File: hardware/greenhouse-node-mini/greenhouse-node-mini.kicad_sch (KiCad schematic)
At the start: 40 parts, among them J1 Molex_KK_396_1x2, J2 JST_XH_2.54mm_1x2, J4 Molex_KK_396_1x2, J5 JST_XH_2.54mm_1x4, J6 PinHeader_1x04_P2.54mm, J7 PinHeader_1x04_P2.54mm, Q1 A42, U1 ATtiny84A-P, U2 L7805, U3 PCF8574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

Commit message: Swapped GND/PWR for IC programming connector
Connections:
- net +5V: now also J2.2 (Pin_2); no longer J2.1 (Pin_1)
- net GND: now also J2.1 (Pin_1); no longer J2.2 (Pin_2)
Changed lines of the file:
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@@
     (pin "1")
+  )
+  (symbol (lib_id "Connector:Conn_01x02_Male") (at 45.72 62.23 0) (mirror x) (unit 1)
+    (in_bom yes) (on_board yes) (fields_autoplaced)
+    (property "Reference" "J2" (id 0) (at 44.45 59.6899 0)
+      (effects (font (size 1.27 1.27)) (justify right))
+    )
+    (property "Value" "JST_XH_2.54mm_1x2" (id 1) (at 44.45 62.2299 0)
+      (effects (font (size 1.27 1.27)) (justify right))
+    )
+    (property "Footprint" "Connector_JST:JST_XH_B2B-XH-A_1x02_P2.50mm_Vertical" (id 2) (at 45.72 62.23 0)
+      (effects (font (size 1.27 1.27)) hide)
+    )
+    (property "Datasheet" "~" (id 3) (at 45.72 62.23 0)
+      (effects (font (size 1.27 1.27)) hide)
+    )
+    (pin "1")
+    (pin "2")
   )
   (symbol (lib_id "power:GND") (at 227.33 133.35 0) (unit 1)
@@
     (pin "2")
   )
-  (symbol (lib_id "Connector:Conn_01x02_Male") (at 45.72 59.69 0) (unit 1)
-    (in_bom yes) (on_board yes) (fields_autoplaced)
-    (property "Reference" "J2" (id 0) (at 46.355 54.61 0))
-    (property "Value" "JST_XH_2.54mm_1x2" (id 1) (at 46.355 57.15 0))
-    (property "Footprint" "Connector_JST:JST_XH_B2B-XH-A_1x02_P2.50mm_Vertical" (id 2) (at 45.72 59.69 0)
-      (effects (font (size 1.27 1.27)) hide)
-    )
-    (property "Datasheet" "~" (id 3) (at 45.72 59.69 0)
-      (effects (font (size 1.27 1.27)) hide)
-    )
-    (pin "1")
-    (pin "2")
-  )
   (symbol (lib_id "Device:R_Small_US") (at 259.08 148.59 270) (mirror x) (unit 1)
     (in_bom yes) (on_board yes) (fields_autoplaced)
@@
       (reference "J1") (unit 1) (value "Molex_KK_396_1x2") (footprint "Connector_Molex:Molex_KK-396_A-41791-0002_1x02_P3.96mm_Vertical")
     )
-    (path "/ea9fe40b-c59e-4c0b-9cb7-bdacd16d2c47"
+    (path "/d9d1085b-9b15-4340-9b95-610882d9fee3"
       (reference "J2") (unit 1) (value "JST_XH_2.54mm_1x2") (footprint "Connector_JST:JST_XH_B2B-XH-A_1x02_P2.50mm_Vertical")
     )

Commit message: Set IO address to 0x20/0x65/0x64
According to internet, 0x20
According to datasheet, 0x65/0x64
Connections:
- net GND: now also U3.1 (A0), U3.2 (A1), U3.3 (A2)
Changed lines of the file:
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@@
   (junction (at 101.6 78.74) (diameter 0) (color 0 0 0 0)
   )
+  (junction (at 147.32 100.33) (diameter 0) (color 0 0 0 0)
+  )
   (junction (at 168.91 30.48) (diameter 0) (color 0 0 0 0)
   )
@@
   (junction (at 57.15 161.29) (diameter 0) (color 0 0 0 0)
   )
+  (junction (at 147.32 102.87) (diameter 0) (color 0 0 0 0)
+  )
   (junction (at 57.15 151.13) (diameter 0) (color 0 0 0 0)
   )
@@
     (stroke (width 0) (type default) (color 0 0 0 0))
   )
+  (wire (pts (xy 147.32 102.87) (xy 153.67 102.87))
+    (stroke (width 0) (type default) (color 0 0 0 0))
+  )
   (wire (pts (xy 255.27 55.88) (xy 266.7 55.88))
     (stroke (width 0) (type default) (color 0 0 0 0))
@@
     (stroke (width 0) (type default) (color 0 0 0 0))
   )
+  (wire (pts (xy 153.67 100.33) (xy 147.32 100.33))
+    (stroke (width 0) (type default) (color 0 0 0 0))
+  )
   (wire (pts (xy 113.03 38.1) (xy 113.03 46.99))
     (stroke (width 0) (type default) (color 0 0 0 0))
@@
     (stroke (width 0) (type default) (color 0 0 0 0))
   )
+  (wire (pts (xy 147.32 97.79) (xy 147.32 100.33))
+    (stroke (width 0) (type default) (color 0 0 0 0))
+  )
   (wire (pts (xy 57.15 151.13) (xy 57.15 140.97))
     (stroke (width 0) (type default) (color 0 0 0 0))
@@
     (stroke (width 0) (type default) (color 0 0 0 0))
   )
+  (wire (pts (xy 147.32 100.33) (xy 147.32 102.87))
+    (stroke (width 0) (type default) (color 0 0 0 0))
+  )
   (wire (pts (xy 175.26 22.86) (xy 175.26 24.13))
     (stroke (width 0) (type default) (color 0 0 0 0))
@@
     (stroke (width 0) (type default) (color 0 0 0 0))
   )
+  (wire (pts (xy 147.32 104.14) (xy 147.32 102.87))
+    (stroke (width 0) (type default) (color 0 0 0 0))
+  )
   (wire (pts (xy 200.66 100.33) (xy 200.66 97.79))
     (stroke (width 0) (type default) (color 0 0 0 0))
@@
   )
   (wire (pts (xy 110.49 46.99) (xy 113.03 46.99))
+    (stroke (width 0) (type default) (color 0 0 0 0))
+  )
+  (wire (pts (xy 153.67 97.79) (xy 147.32 97.79))
     (stroke (width 0) (type default) (color 0 0 0 0))
   )
@@
     (pin "2")
   )
+  (symbol (lib_id "power:GND") (at 147.32 104.14 0) (unit 1)
+    (in_bom yes) (on_board yes) (fields_autoplaced)
+    (property "Reference" "#PWR?" (id 0) (at 147.32 110.49 0)
+      (effects (font (size 1.27 1.27)) hide)
+    )
+    (property "Value" "GND" (id 1) (at 147.32 109.22 0))
+    (property "Footprint" "" (id 2) (at 147.32 104.14 0)
+      (effects (font (size 1.27 1.27)) hide)
+    )
+    (property "Datasheet" "" (id 3) (at 147.32 104.14 0)
+      (effects (font (size 1.27 1.27)) hide)
+    )
+    (pin "1")
+  )
   (symbol (lib_id "power:GND") (at 252.73 130.81 0) (unit 1)
     (in_bom yes) (on_board yes) (fields_autoplaced)
@@
       (reference "#PWR0112") (unit 1) (value "GND") (footprint "")
     )
+    (path "/50bae16a-a78d-43ed-9cff-a3bd02aff6fa"
+      (reference "#PWR?") (unit 1) (value "GND") (footprint "")
+    )
     (path "/695ccbcc-4a44-4a1f-b5e4-e7c0459755d8"

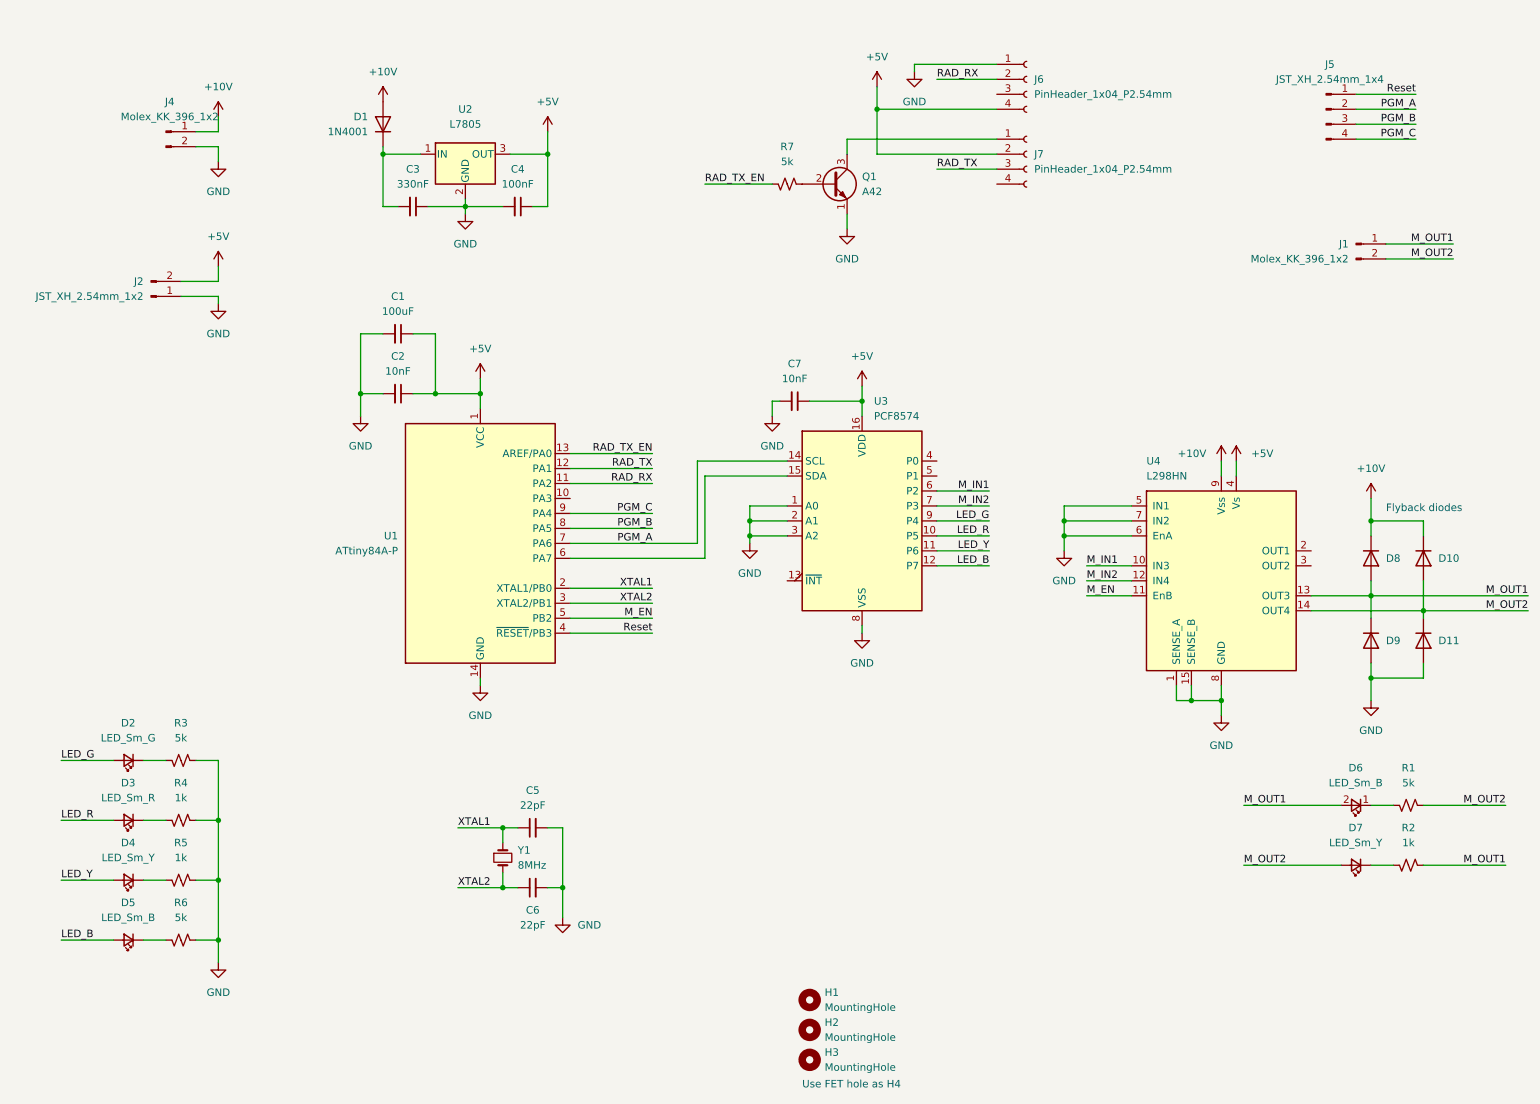
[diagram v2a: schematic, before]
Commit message: Add I2C pull-ups
Also reorganised schematic
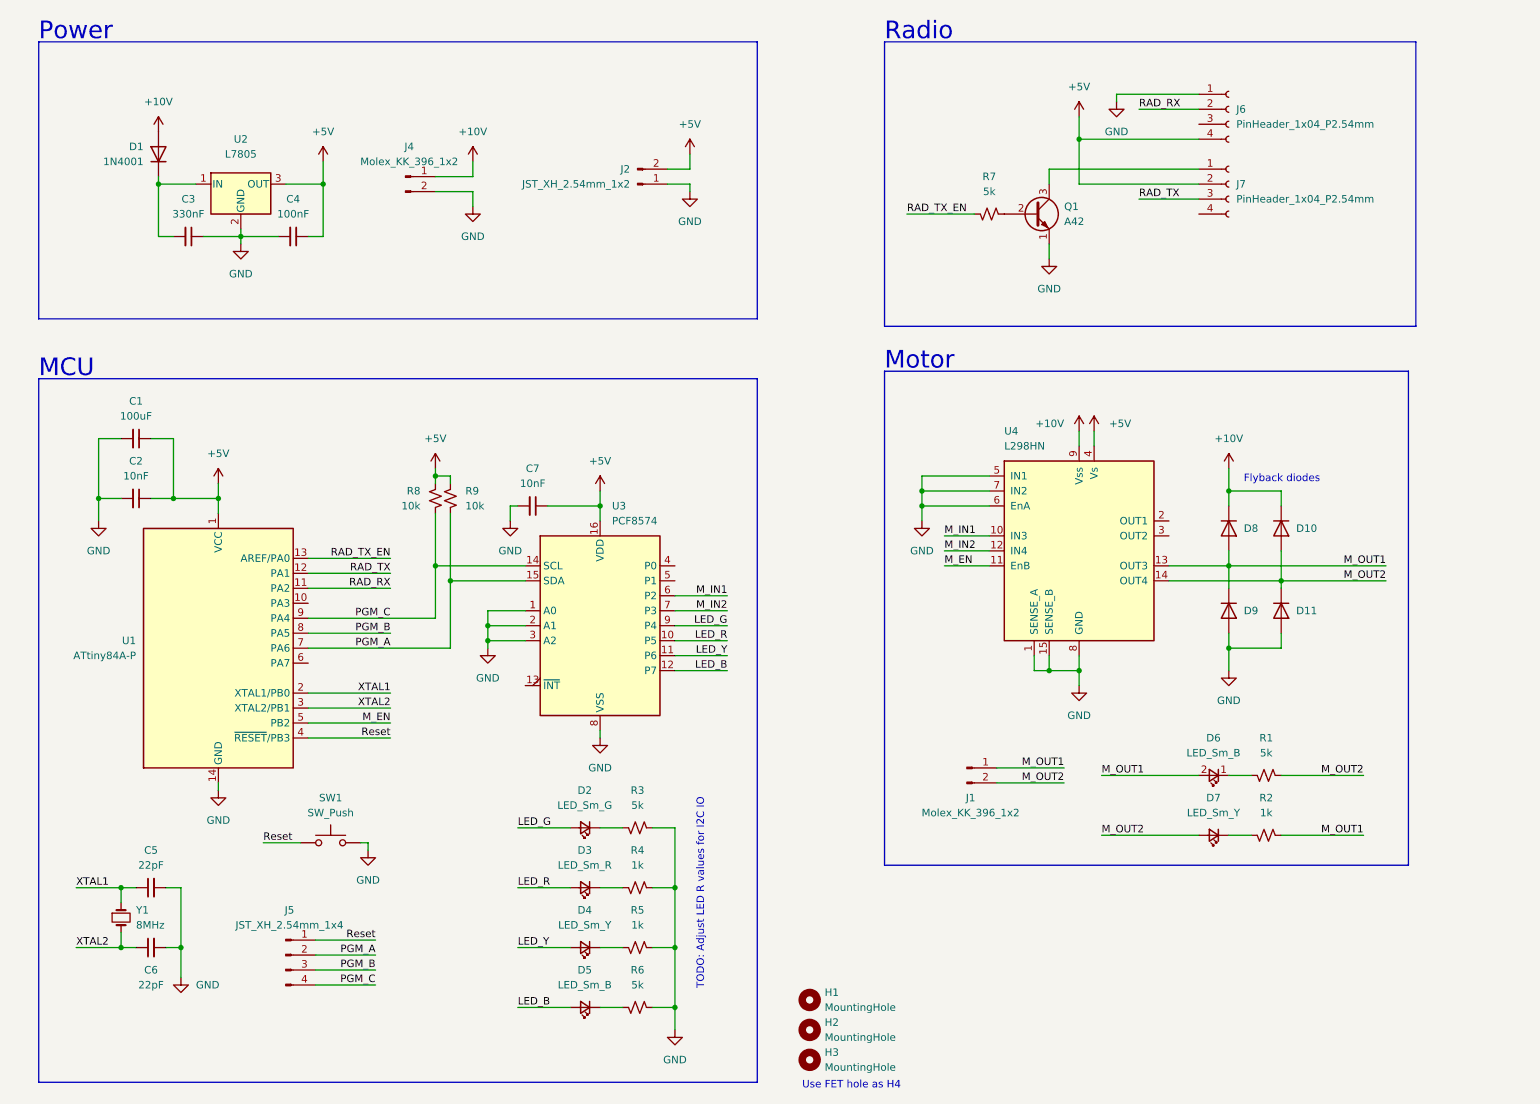
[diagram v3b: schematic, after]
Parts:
- added R8, R9: 10k, Resistor_THT:R_Axial_DIN0204_L3.6mm_D1.6mm_P7.62mm_Horizontal, symbol Device:R_Small_US
- added SW1: SW_Push, Button_Switch_THT:SW_PUSH_6mm, symbol Switch:SW_Push
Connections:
- net +5V: now also R8.1, R9.1
- net GND: now also SW1.2
- net PGM_A: now also U3.15 (SDA), R9.2; no longer U3.14 (SCL)
- net PGM_C: now also U3.14 (SCL), R8.2
- net Reset: now also SW1.1
- net at U1.6 (PA7): no longer U3.15 (SDA)
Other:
- note added: "MCU"
- note added: "Motor"
- note added: "Power"
- note added: "Radio"
- note added: "TODO: Adjust LED R values for I2C IO"
- company: (none) -> Nick Bolton
- title: (none) -> Greenhouse Node Mini
- moved on the sheet: C1, C2, C3, C4, C5, C6, C7, D1, D10, D11, D2, D3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

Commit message: Change LEDs to current sink (PCB WIP)
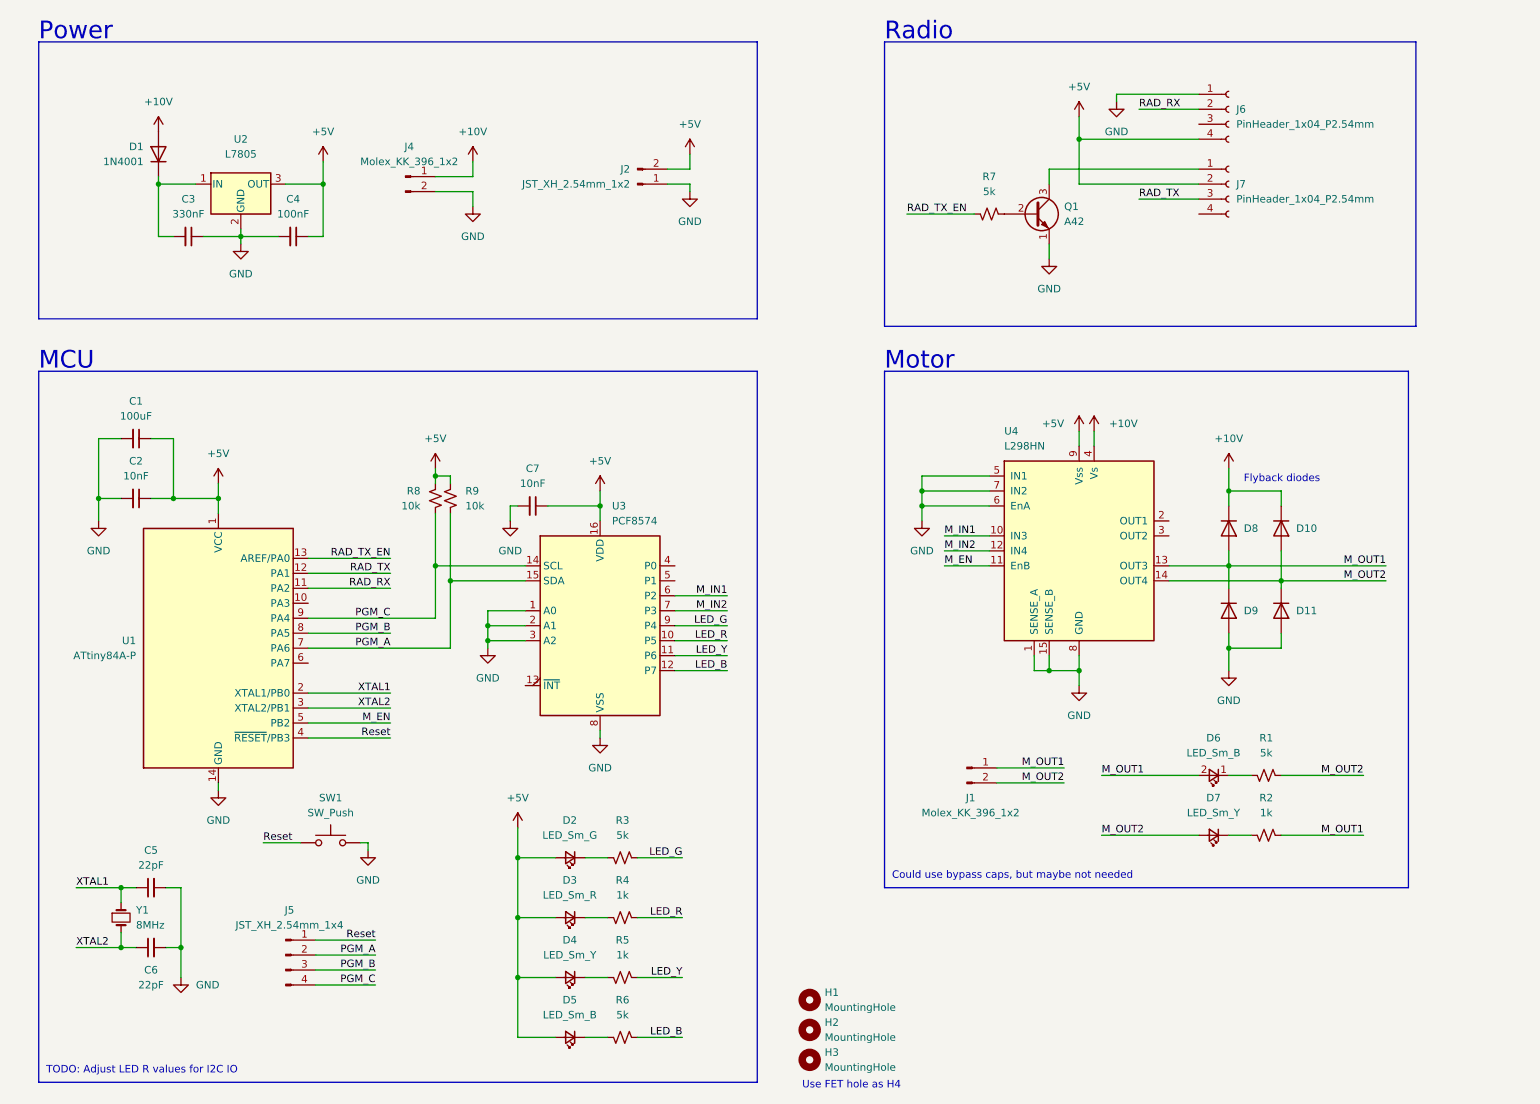
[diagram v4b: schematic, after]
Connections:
- net +10V: now also U4.4 (Vs); no longer U4.9 (Vss)
- net +5V: now also D2.2 (A), D3.2 (A), D4.2 (A), D5.2 (A), U4.9 (Vss); no longer U4.4 (Vs)
- net GND: no longer R3.1, R4.1, R5.1, R6.1
- net LED_B: now also R6.1; no longer D5.2 (A)
- net LED_G: now also R3.1; no longer D2.2 (A)
- net LED_R: now also R4.1; no longer D3.2 (A)
- net LED_Y: now also R5.1; no longer D4.2 (A)
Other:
- note added: "Could use bypass caps, but maybe not needed"
- moved on the sheet: D2, D3, D4, D5

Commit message: Change diodes to fast recovery
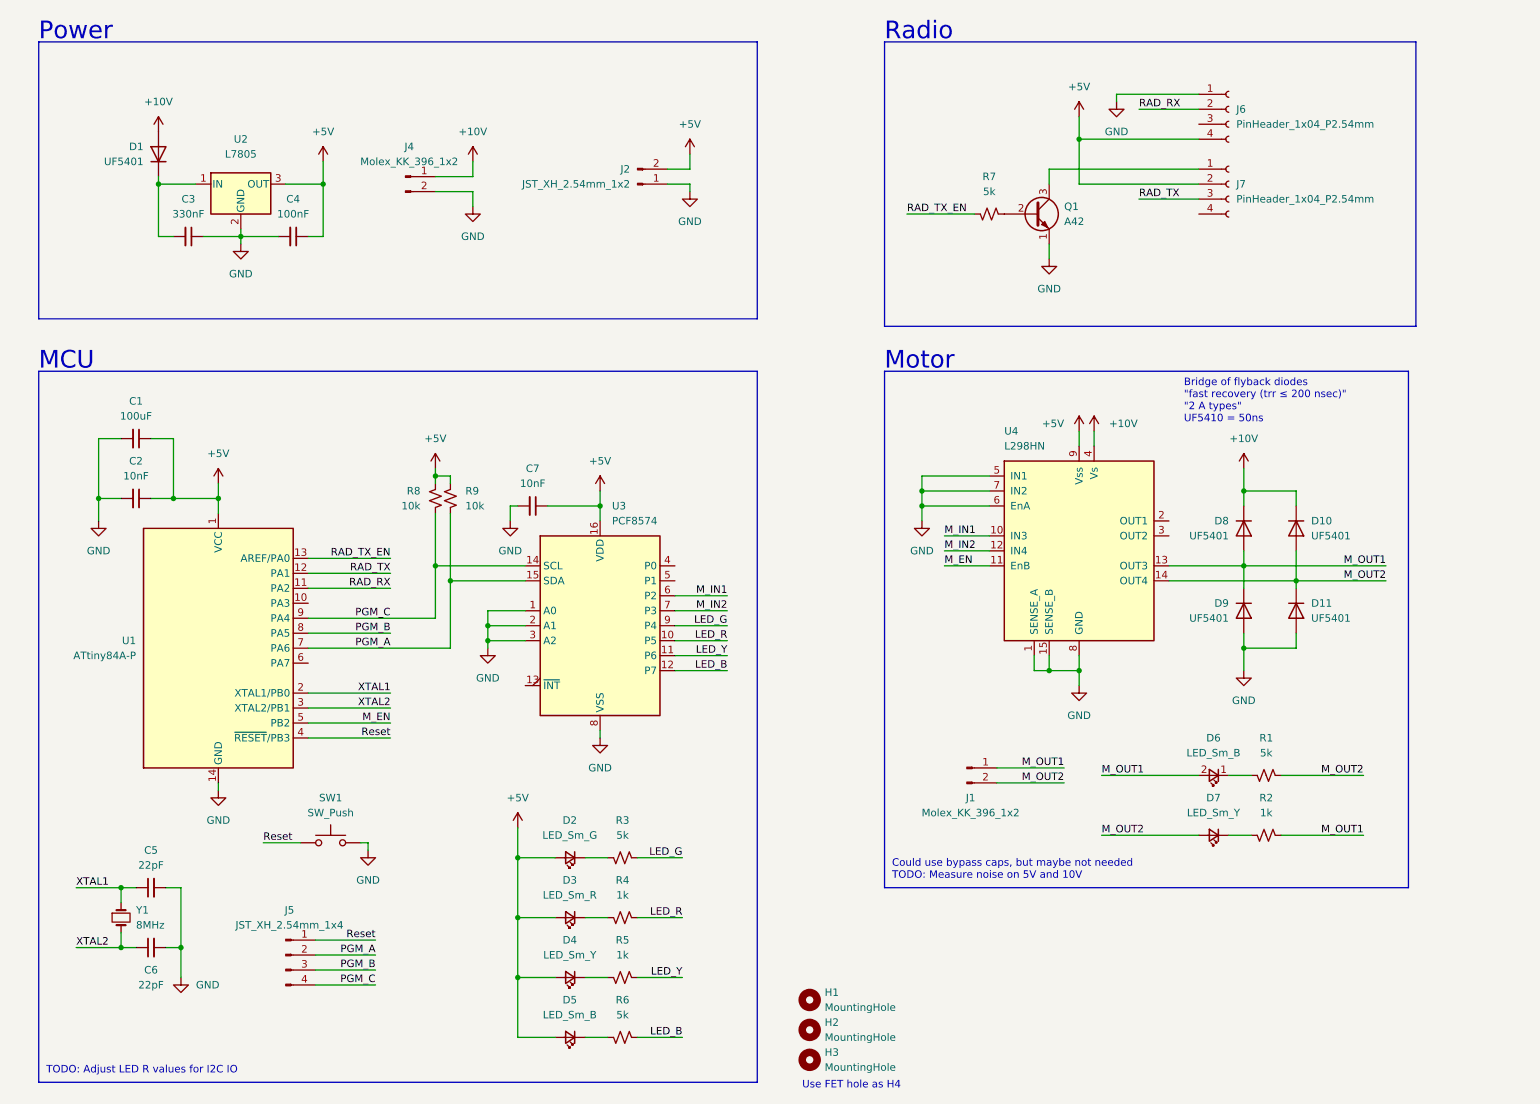
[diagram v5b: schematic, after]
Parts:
- D1: value 1N4001 -> UF5401; footprint Diode_THT:D_DO-41_SOD81_P7.62mm_Horizontal -> Diode_THT:D_DO-201AD_P15.24mm_Horizontal; symbol Diode:1N4001 -> Diode:UF5401
- D10, D11, D8, D9: value 1N4007 -> UF5401; footprint Diode_THT:D_DO-41_SOD81_P7.62mm_Horizontal -> Diode_THT:D_DO-201AD_P15.24mm_Horizontal; symbol Diode:1N4001 -> Diode:UF5401
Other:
- note added: "Bridge of flyback diodes "fast recovery (trr ≤ 200 nsec)" "2 A types" UF5410 = 50ns"
- note added: "Could use bypass caps, but maybe not needed TODO: Measure noise on 5V and 10V"
- note removed: "Could use bypass caps, but maybe not needed"
- note removed: "Flyback diodes"
- moved on the sheet: D10, D11, D8, D9
